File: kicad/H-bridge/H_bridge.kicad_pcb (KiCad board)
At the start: 2 copper layers, 127 x 63.5 mm, 69 parts, among them J1 Screw_Terminal_01x03, J2 Conn_Coaxial, J3 2453710000, J4 Screw_Terminal_01x02, Q1 IAUT300N10S5N014ATMA1, Q2 IAUT300N10S5N014ATMA1, Q3 IAUT300N10S5N014ATMA1, Q4 IAUT300N10S5N014ATMA1, U1 LTV-817, U2 PDS1-S15-S15-M, U3 HIP4080A, U4 LT1011, U5 LM340MPX-5.0/NOPB, U6 74LVC1G373, U8 74AC14DR

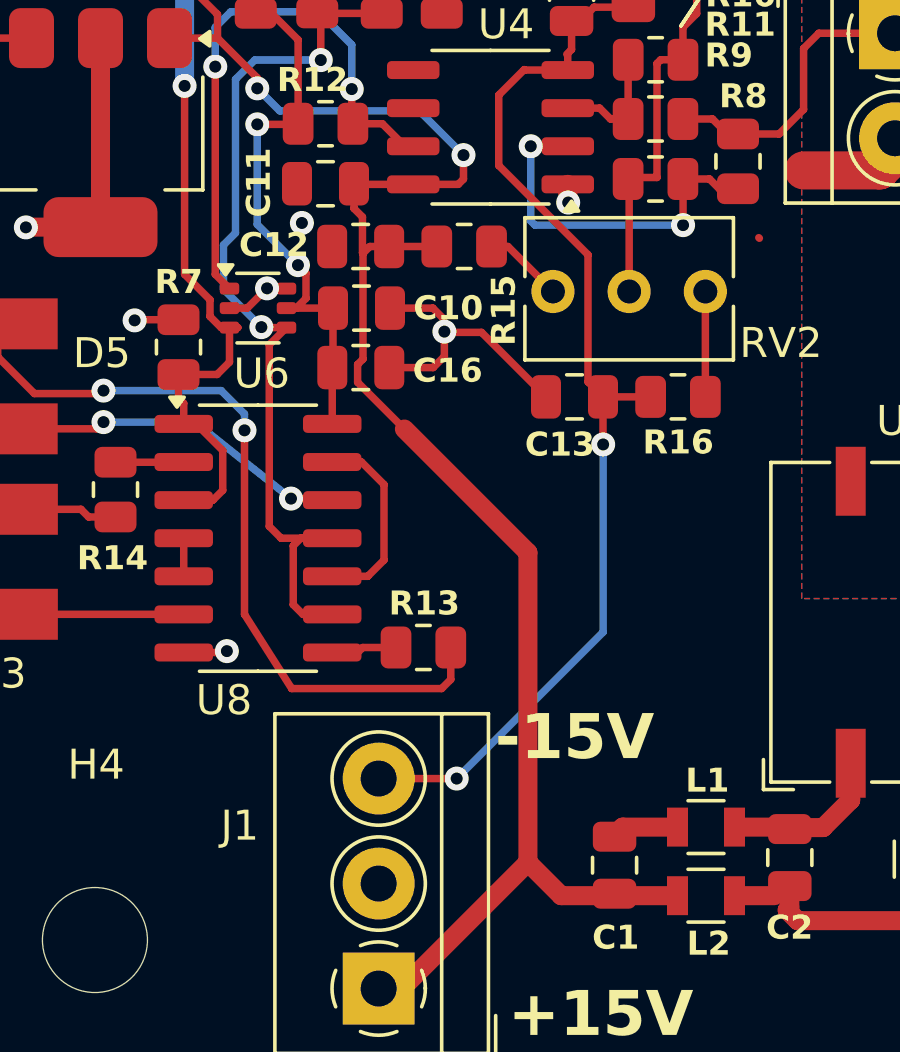
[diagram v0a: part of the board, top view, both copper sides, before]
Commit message: Final Board schematics and layouts, Also added custom footprints that were made for the relay and terminal connector block.
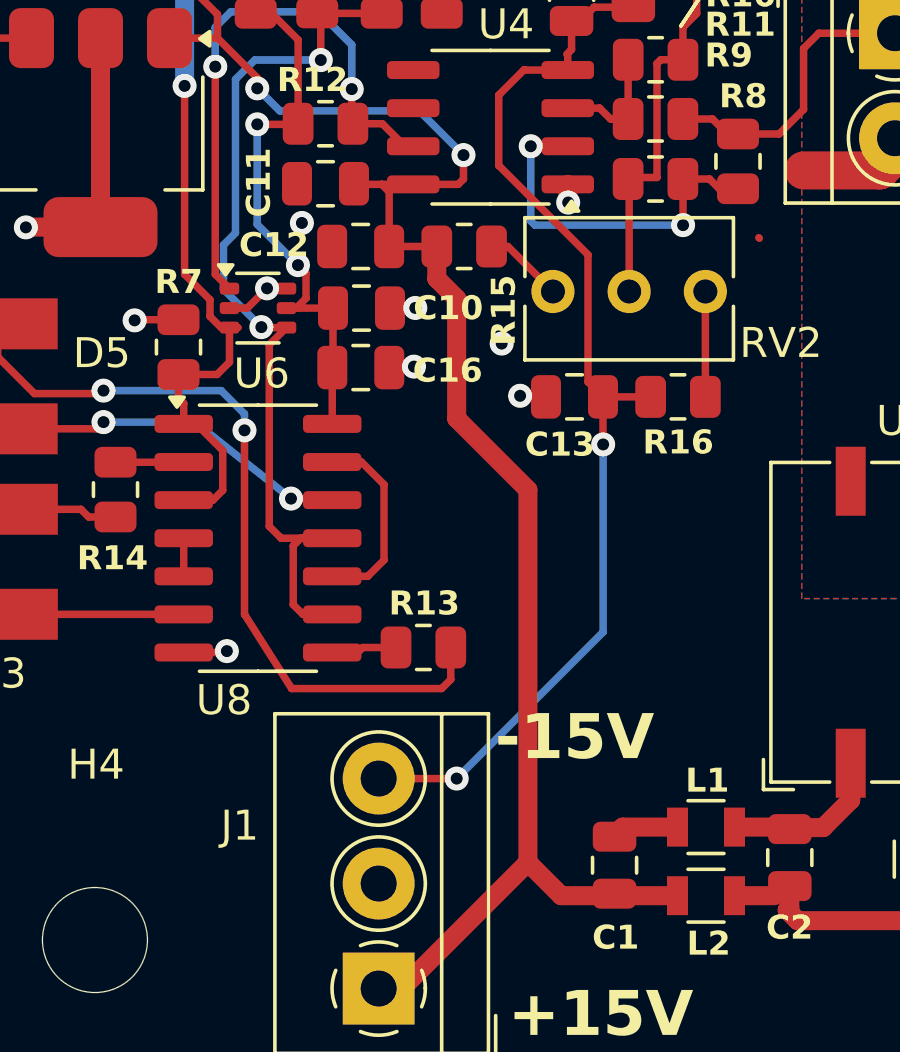
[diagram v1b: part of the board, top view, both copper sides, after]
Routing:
- net GND: track 33.4 -> 23.9 mm, vias 9 -> 12
- net VCC: track 58.9 -> 56.7 mm
